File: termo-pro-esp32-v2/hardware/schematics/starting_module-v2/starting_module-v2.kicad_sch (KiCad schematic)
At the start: 10 parts, among them K1 SANYOU_SRD_Form_C, Q1 PN2222A, U1 ESP32-DevKitC

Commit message: schematic redone and improvment.
more to come...
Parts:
- added C2: 50V 220nF, symbol Device:C
- added J1: Screw_Terminal_01x02, symbol Connector:Screw_Terminal_01x02
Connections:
- net +VDC: now also C2.2
- net -VDC: now also C2.1
- net at K1.1: now also J1.2 (Pin_2); no longer K1.3
- new net: J1.1 (Pin_1), K1.3
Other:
- moved on the sheet: D3

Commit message: *
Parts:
- removed C2: 50V 220nF, symbol Device:C
- removed U1: ESP32-DevKitC, PCM_Espressif:ESP32-DevKitC, symbol ESP32-All:ESP32-DevKitC
- added C3: 50V 220nF, Capacitor_THT:C_Radial_D10.0mm_H12.5mm_P5.00mm, symbol Device:C
- added D4: LED, LED_THT:LED_D5.0mm_FlatTop, symbol Device:LED
- added R4: 1k, Resistor_THT:R_Axial_DIN0207_L6.3mm_D2.5mm_P7.62mm_Horizontal, symbol Device:R
- added SW1: SW_SPDT, Button_Switch_THT:SW_Slide_SPDT_Straight_CK_OS102011MS2Q, symbol Switch:SW_SPDT
- added U1: (no value), ESP32-C3_SUPERMINI_TH:MODULE_ESP32-C3_SUPERMINI_TH, symbol ESP32-C3-SuperMini:ESP32-C3-SuperMini
- C1: footprint (none) -> Capacitor_THT:CP_Radial_D8.0mm_P5.00mm
- D1, D2: footprint (none) -> LED_THT:LED_D5.0mm_FlatTop
- J1: footprint (none) -> TerminalBlock_Phoenix:TerminalBlock_Phoenix_MKDS-1,5-2-5.08_1x02_P5.08mm_Horizontal
- R1, R2: value 220 -> 470; footprint (none) -> Resistor_THT:R_Axial_DIN0207_L6.3mm_D2.5mm_P7.62mm_Horizontal
- R3: value 1k -> 330; footprint (none) -> Resistor_THT:R_Axial_DIN0207_L6.3mm_D2.5mm_P7.62mm_Horizontal
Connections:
- net +VDC: now also C3.2, R4.1, U1.8 (5V)
- net -VDC: now also C3.1, SW1.3 (C), U1.9 (GND)
- net at R2.2: now also U1.2 (GPIO6)
- net at D3.2 (A), Q1.3 (C): now also SW1.1 (A); no longer K1.2
- net at R1.2: now also U1.3 (GPIO7)
- net at R3.2: now also U1.1 (ADC2/GPIO5)
- new net: D4.2 (A), R4.2
- new net: D4.1 (K), K1.2, SW1.2 (B)
- no-connect marks 32 -> 16
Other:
- note added: "alpha 0.4"
- note removed: "alpha 0.2"
- moved on the sheet: C1, D1, D2, D3, J1, K1, R1, R2

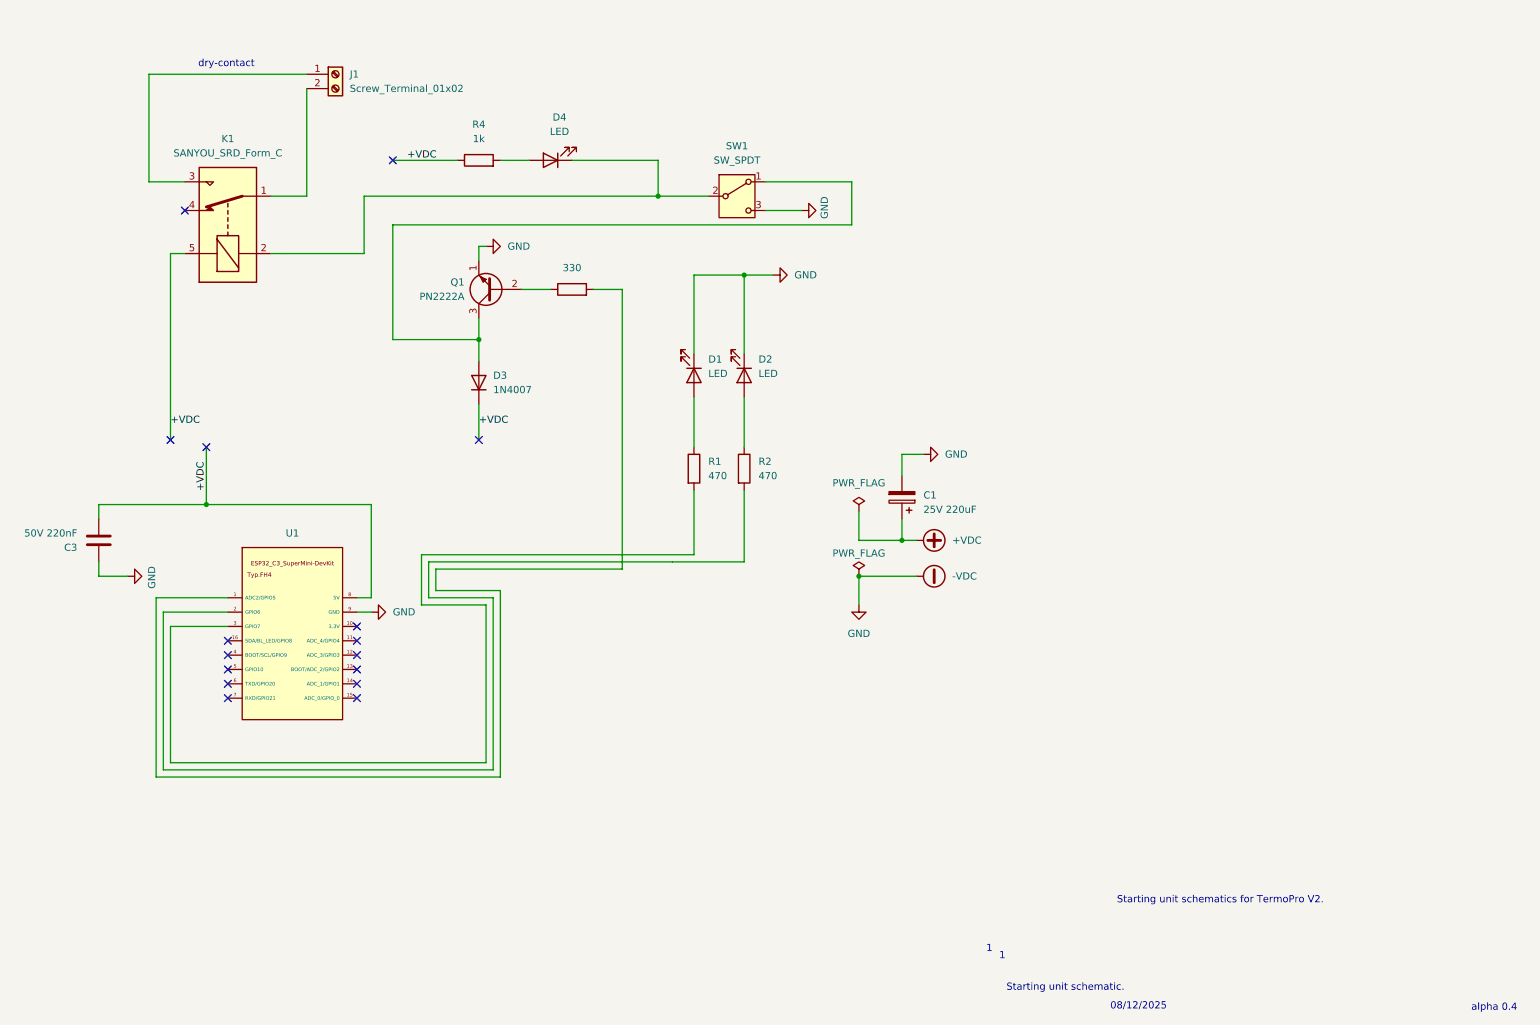
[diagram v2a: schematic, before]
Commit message: Firmware modification and complete schematics redone and improvement.
All schematics have been redone.
All components have footprints.
Microcontrollers  used ESP32S-38 NodeMCU and ESP32-C3-SuperMini.

ESP8266 has been eliminated because of compatibility issues.

Next phase is PCB design.
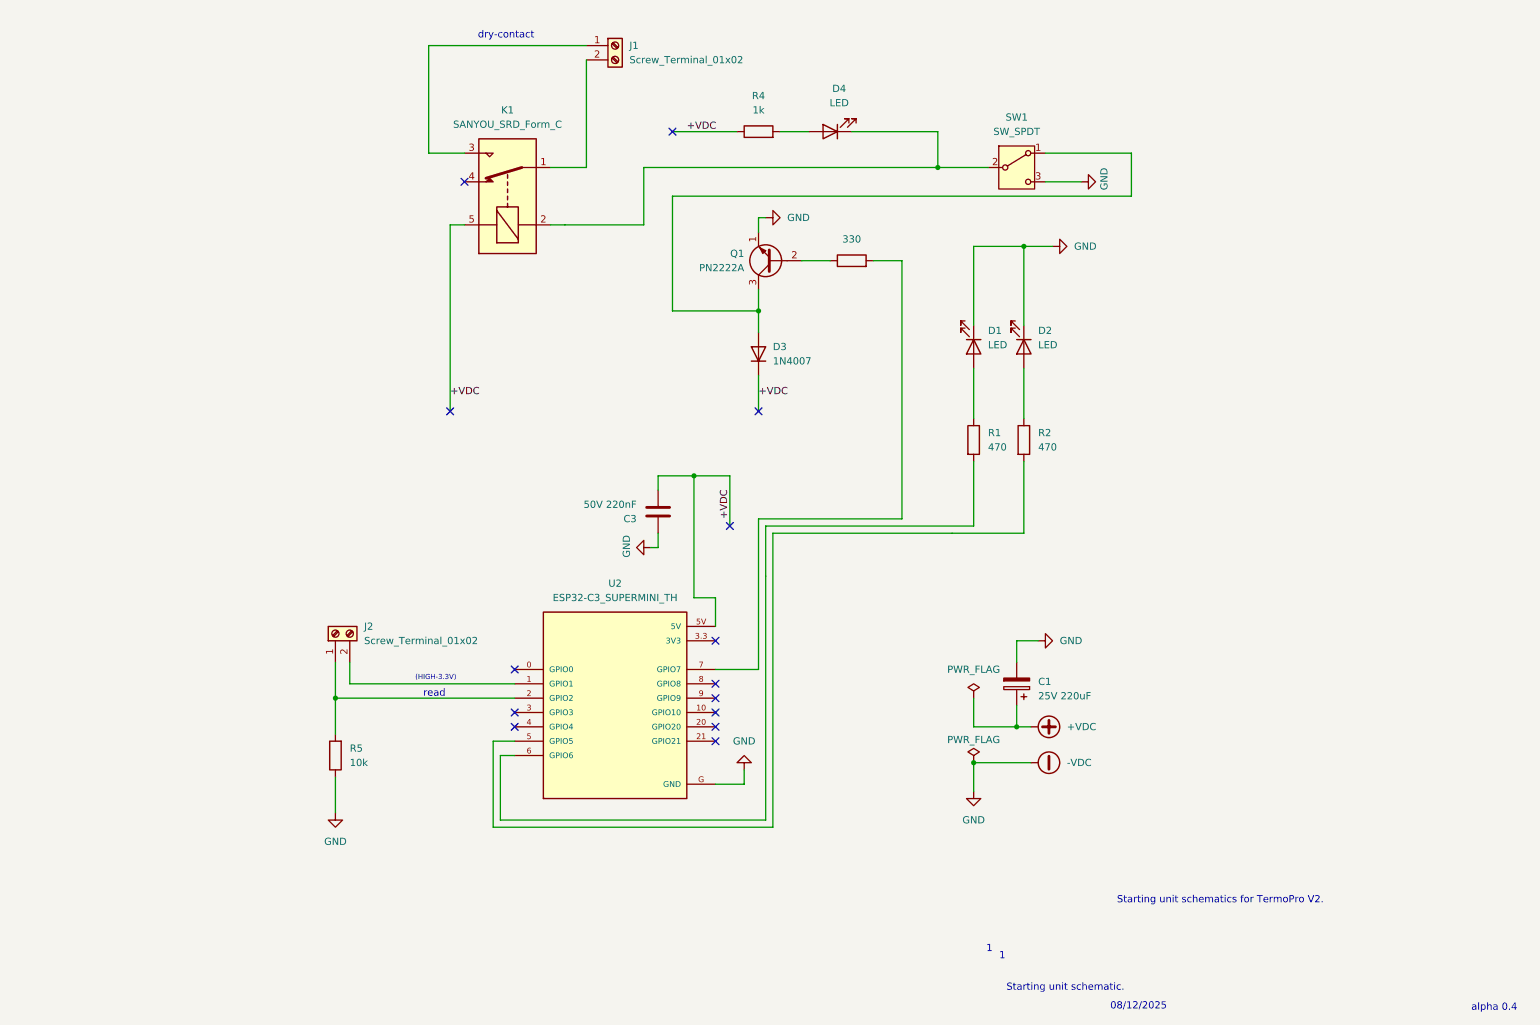
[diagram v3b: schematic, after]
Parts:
- removed U1: (no value), ESP32-C3_SUPERMINI_TH:MODULE_ESP32-C3_SUPERMINI_TH, symbol ESP32-C3-SuperMini:ESP32-C3-SuperMini
- added J2: Screw_Terminal_01x02, TerminalBlock_Phoenix:TerminalBlock_Phoenix_MKDS-1,5-2-5.08_1x02_P5.08mm_Horizontal, symbol Connector:Screw_Terminal_01x02
- added R5: 10k, Resistor_THT:R_Axial_DIN0207_L6.3mm_D2.5mm_P7.62mm_Horizontal, symbol Device:R
- added U2: ESP32-C3_SUPERMINI_TH, ESP32-C3_SUPERMINI_TH:MODULE_ESP32-C3_SUPERMINI_TH, symbol ESP32-C3_SUPERMINI_TH:ESP32-C3_SUPERMINI_TH
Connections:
- net +VDC: now also U2.5V
- net -VDC: now also R5.1, U2.G (GND)
- net at R2.2: now also U2.5 (GPIO5)
- net at R3.2: now also U2.7 (GPIO7)
- net at R1.2: now also U2.6 (GPIO6)
- new net: J2.2 (Pin_2), U2.1 (GPIO1)
- new net: J2.1 (Pin_1), R5.2, U2.2 (GPIO2)
- no-connect marks 16 -> 14
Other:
- note added: "(HIGH-3.3V)"
- note added: "read"
- moved on the sheet: C1, C3, D1, D2, D3, D4, J1, K1, Q1, R1, R2, R4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

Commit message: Final schematics and footprints for all components.
- All schematics have been completed.
- All components have footprints.

Next:
- Testing schematics for any errors phisically.
- Making PCBs based on schmatics.
- Android app for termostat parameteers control.
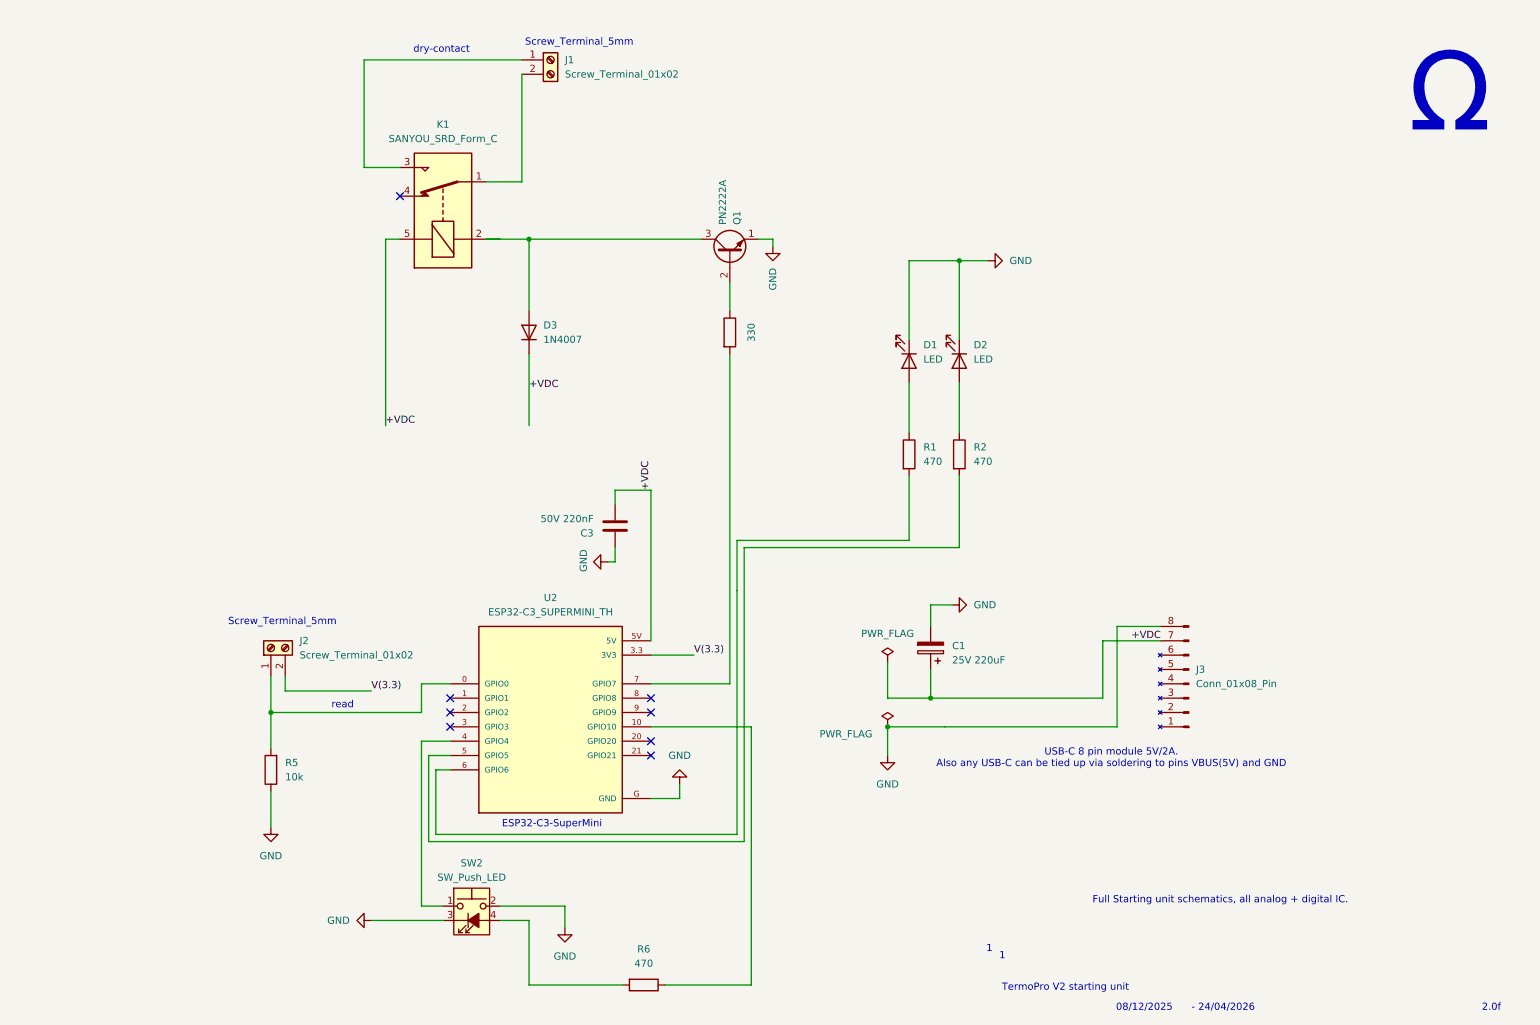
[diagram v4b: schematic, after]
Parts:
- removed D4: LED, LED_THT:LED_D5.0mm_FlatTop, symbol Device:LED
- removed R4: 1k, Resistor_THT:R_Axial_DIN0207_L6.3mm_D2.5mm_P7.62mm_Horizontal, symbol Device:R
- removed SW1: SW_SPDT, Button_Switch_THT:SW_Slide_SPDT_Straight_CK_OS102011MS2Q, symbol Switch:SW_SPDT
- added J3: Conn_01x08_Pin, Connector_PinHeader_2.54mm:PinHeader_1x08_P2.54mm_Vertical, symbol Connector:Conn_01x08_Pin
- added R6: 470, Resistor_THT:R_Axial_DIN0207_L6.3mm_D2.5mm_P10.16mm_Horizontal, symbol Device:R
- added SW2: SW_Push_LED, SW_PUSH_THT_12mm:SW_PUSH-12mm, symbol Switch:SW_Push_LED
- R1, R2, R3, R5: footprint Resistor_THT:R_Axial_DIN0207_L6.3mm_D2.5mm_P7.62mm_Horizontal -> Resistor_THT:R_Axial_DIN0207_L6.3mm_D2.5mm_P10.16mm_Horizontal
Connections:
- net +VDC: now also J3.7 (VBUS)
- net at D3.2 (A), Q1.3 (C): now also K1.2
- net at U2.0 (GPIO0): now also J2.1 (Pin_1), R5.2
- net at U2.1 (GPIO1): no longer J2.2 (Pin_2)
- net at U2.10 (GPIO10): now also R6.1
- net V(3.3): now reaches U2.3.3 (3V3)
- net V(3.3): now also J2.2 (Pin_2)
- net at U2.4 (GPIO4): now also SW2.1
- net -VDC renamed GND
- net GND: now also J3.8 (GND), SW2.2, SW2.3 (K)
- new net: R6.2, SW2.4 (A)
- now unconnected: U2.2 (GPIO2)
- no-connect marks 14 -> 8
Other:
- note added: "- 24/04/2026"
- note added: "2.0f"
- note added: "ESP32-C3-SuperMini"
- note added: "Full Starting unit schematics, all analog + digital IC."
- note added: "Screw_Terminal_5mm"
- note added: "TermoPro V2 starting unit"
- note added: "USB-C 8 pin module 5V/2A. Also any USB-C can be tied up via soldering to pins VBUS(5V) and GND"
- note added: "Ω"
- note removed: "(HIGH-3.3V)"
- note removed: "Starting unit schematic."
- note removed: "Starting unit schematics for TermoPro V2."
- note removed: "alpha 0.4"
- moved on the sheet: C1, C3, D1, D2, J1, J2, K1, Q1, R1, R2, R5, U2

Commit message: Starting Unit PCB compleate.
Some footprint issues were encountered on the initial unit PCB, regarding the ceramic capacitors and the 1×02 5.08 mm screw terminal.

-In the thermostat schematic, the ceramic capacitors were updated to a disc footprint , as well in the starting unit scheme.

-Thermostat PCB is currently in progress.
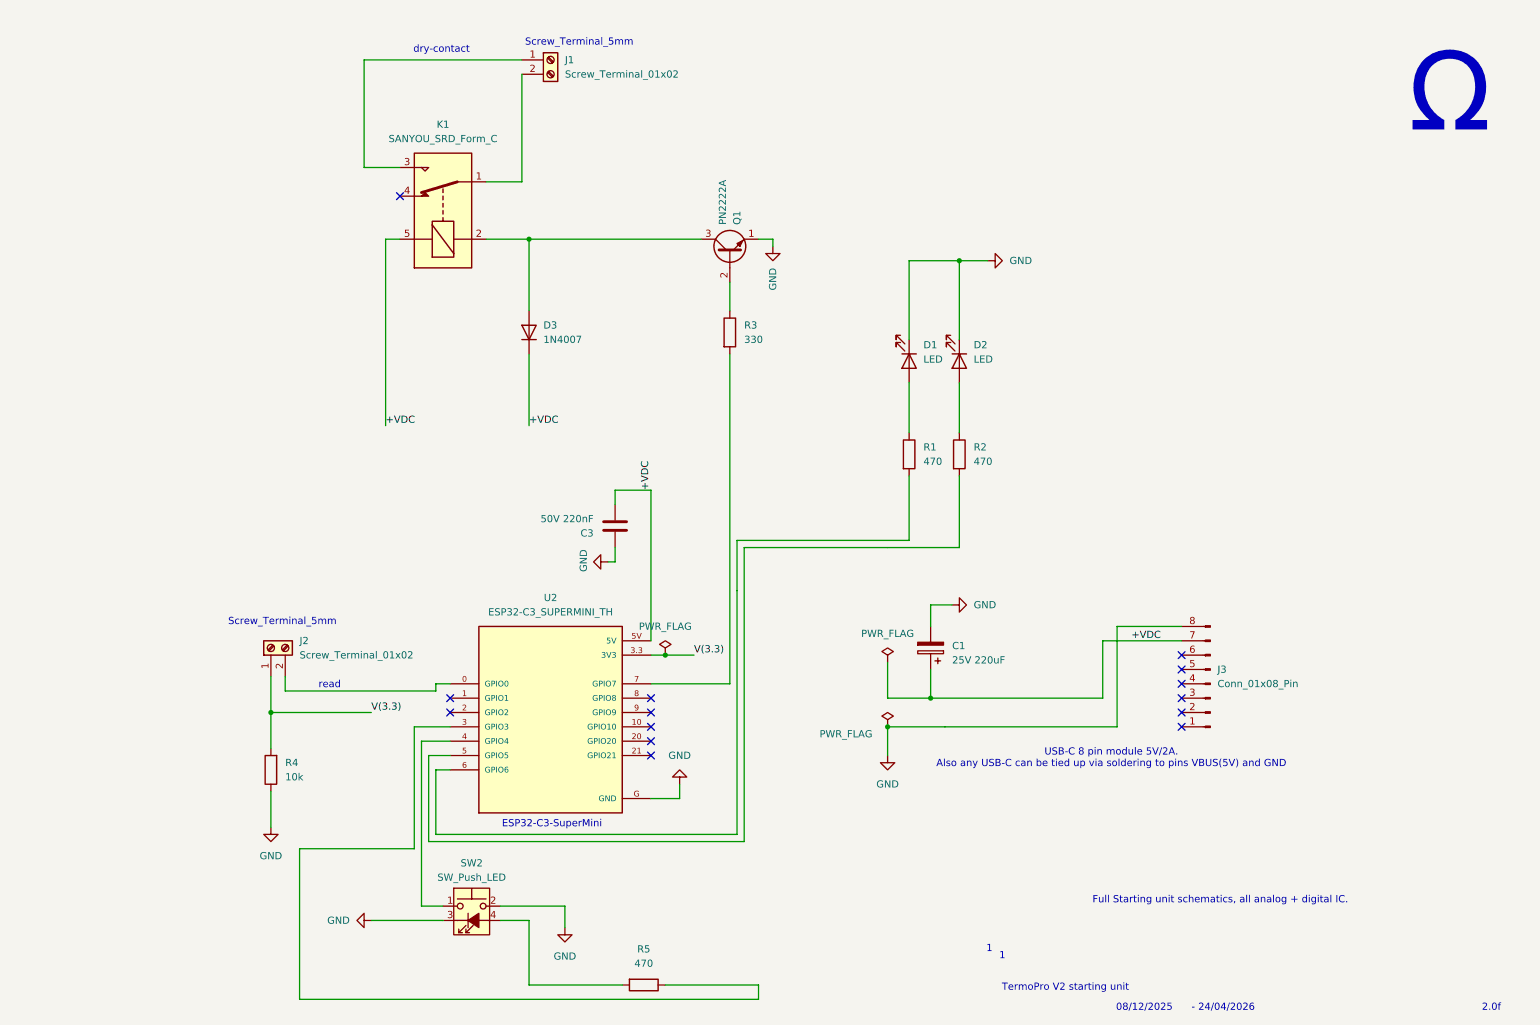
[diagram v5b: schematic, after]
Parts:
- C3: footprint Capacitor_THT:C_Radial_D10.0mm_H12.5mm_P5.00mm -> Capacitor_THT:C_Disc_D11.0mm_W5.0mm_P5.00mm
- J1, J2: footprint TerminalBlock_Phoenix:TerminalBlock_Phoenix_MKDS-1,5-2-5.08_1x02_P5.08mm_Horizontal -> TerminalBlock_RND:TerminalBlock_RND_205-00232_1x02_P5.08mm_Horizontal
- J3: footprint Connector_PinHeader_2.54mm:PinHeader_1x08_P2.54mm_Vertical -> Connector_PinSocket_2.54mm:PinSocket_1x08_P2.54mm_Vertical
- renumbered R5 to R4, R6 to R5
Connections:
- net V(3.3): now also J2.1 (Pin_1), R4.2; no longer J2.2 (Pin_2)
- net at U2.10 (GPIO10): no longer R5.1
- net at U2.3 (GPIO3): now also R5.1
- new net: J2.2 (Pin_2), U2.0 (GPIO0)
- no-connect marks 8 -> 14

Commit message: *
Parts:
- removed J3: Conn_01x08_Pin, Connector_PinSocket_2.54mm:PinSocket_1x08_P2.54mm_Vertical, symbol Connector:Conn_01x08_Pin
- removed R5: 470, Resistor_THT:R_Axial_DIN0207_L6.3mm_D2.5mm_P10.16mm_Horizontal, symbol Device:R
- removed SW2: SW_Push_LED, SW_PUSH_THT_12mm:SW_PUSH-12mm, symbol Switch:SW_Push_LED
- added D4: LED, LED_THT:LED_D5.0mm_FlatTop, symbol Device:LED
- added R4: 1k, Resistor_THT:R_Axial_DIN0207_L6.3mm_D2.5mm_P7.62mm_Horizontal, symbol Device:R
- added SW1: SW_SPDT, Button_Switch_THT:SW_Slide_SPDT_Straight_CK_OS102011MS2Q, symbol Switch:SW_SPDT
- C3: footprint Capacitor_THT:C_Disc_D11.0mm_W5.0mm_P5.00mm -> Capacitor_THT:C_Radial_D10.0mm_H12.5mm_P5.00mm
- J1, J2: footprint TerminalBlock_RND:TerminalBlock_RND_205-00232_1x02_P5.08mm_Horizontal -> TerminalBlock_Phoenix:TerminalBlock_Phoenix_MKDS-1,5-2-5.08_1x02_P5.08mm_Horizontal
- R1, R2, R3: footprint Resistor_THT:R_Axial_DIN0207_L6.3mm_D2.5mm_P10.16mm_Horizontal -> Resistor_THT:R_Axial_DIN0207_L6.3mm_D2.5mm_P7.62mm_Horizontal
- R5: renamed from R4; footprint Resistor_THT:R_Axial_DIN0207_L6.3mm_D2.5mm_P10.16mm_Horizontal -> Resistor_THT:R_Axial_DIN0207_L6.3mm_D2.5mm_P7.62mm_Horizontal
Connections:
- net +VDC: now also R4.1
- net at D3.2 (A), Q1.3 (C): now also SW1.1 (A); no longer K1.2
- net at U2.0 (GPIO0): no longer J2.2 (Pin_2)
- net at U2.1 (GPIO1): now also J2.2 (Pin_2)
- net at U2.2 (GPIO2): now also J2.1 (Pin_1), R5.2
- net GND renamed -VDC
- net -VDC: now also SW1.3 (C)
- removed net V(3.3): J2.1 (Pin_1), R5.2, U2.3.3 (3V3)
- new net: D4.2 (A), R4.2
- new net: D4.1 (K), K1.2, SW1.2 (B)
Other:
- note added: "(HIGH-3.3V)"
- note added: "Starting unit schematic."
- note added: "Starting unit schematics for TermoPro V2."
- note added: "alpha 0.4"
- note removed: "- 24/04/2026"
- note removed: "2.0f"
- note removed: "ESP32-C3-SuperMini"
- note removed: "Full Starting unit schematics, all analog + digital IC."
- note removed: "Screw_Terminal_5mm"
- note removed: "TermoPro V2 starting unit"
- note removed: "USB-C 8 pin module 5V/2A. Also any USB-C can be tied up via soldering to pins VBUS(5V) and GND"
- note removed: "Ω"
- moved on the sheet: C1, C3, D1, D2, J1, J2, K1, Q1, R1, R2, R5, U2
